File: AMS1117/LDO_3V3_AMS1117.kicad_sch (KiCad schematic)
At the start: 5 parts, among them U1 AMS1117-3.3

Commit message: added gnd
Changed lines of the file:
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@@
+	(wire
+		(pts
+			(xy 170.18 110.49) (xy 170.18 109.22)
+		)
+		(stroke
+			(width 0)
+			(type default)
+		)
+	)
 	(wire
 		(pts
@@
 		(pts
 			(xy 163.83 95.25) (xy 163.83 96.52)
+		)
+		(stroke
+			(width 0)
+			(type default)
+		)
+	)
+	(wire
+		(pts
+			(xy 170.18 109.22) (xy 172.72 109.22)
 		)
 		(stroke
@@
 		(shape input)
 		(at 125.73 95.25 90)
+		(fields_autoplaced yes)
+		(effects
+			(font
+				(size 1.27 1.27)
+			)
+			(justify left)
+		)
+	)
+	(hierarchical_label "GND"
+		(shape bidirectional)
+		(at 172.72 109.22 0)
 		(fields_autoplaced yes)
 		(effects
@@
 					(unit 1)
 				)
+			)
+		)
+	)
+	(symbol
+		(lib_id "power:GND")
+		(at 170.18 110.49 0)
+		(unit 1)
+		(exclude_from_sim no)
+		(in_bom yes)
+		(on_board yes)
+		(dnp no)
+		(property "Reference" "#PWR01"
+			(at 170.18 116.84 0)
+			(effects
+				(font
+					(size 1.27 1.27)
+				)
+				(hide yes)
+			)
+		)
+		(property "Value" "GND"
+			(at 170.307 114.8842 0)
+			(effects
+				(font
+					(size 1.27 1.27)
+				)
+			)
+		)
+		(property "Footprint" ""
+			(at 170.18 110.49 0)
+			(effects
+				(font
+					(size 1.27 1.27)
+				)
+				(hide yes)
+			)
+		)
+		(property "Datasheet" ""
+			(at 170.18 110.49 0)
+			(effects
+				(font
+					(size 1.27 1.27)
+				)
+				(hide yes)
+			)
+		)
+		(property "Description" ""
+			(at 170.18 110.49 0)
+			(effects
+				(font
+					(size 1.27 1.27)
+				)
+				(hide yes)
+			)
+		)
+		(pin "1"
+		)
+		(instances
+			(project "AMS1117"
+				(path "/d6eee423-2a55-45ad-a749-7df2395c1501/18c18bcb-7cad-4433-83e1-269ce5efd3b2"
+					(reference "#PWR01")
+					(unit 1)
+				)

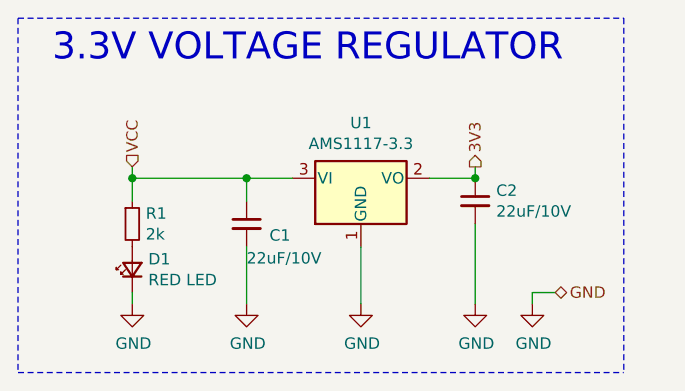
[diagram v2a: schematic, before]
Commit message: changes in, out for ams1117
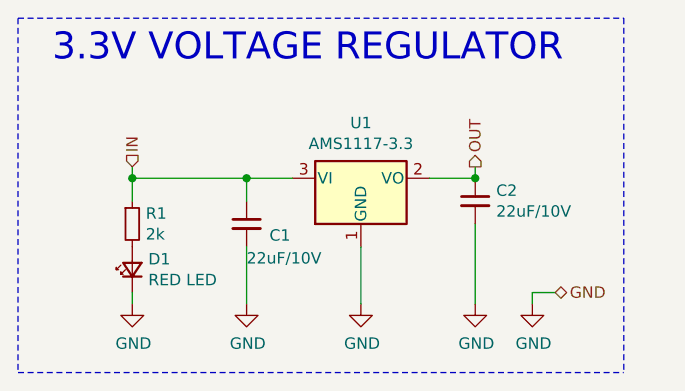
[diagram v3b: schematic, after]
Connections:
- net 3V3 renamed OUT
- net VCC renamed IN
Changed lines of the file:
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@@
 		)
 	)
-	(hierarchical_label "VCC"
+	(hierarchical_label "IN"
 		(shape input)
 		(at 125.73 95.25 90)
@@
 		)
 	)
-	(hierarchical_label "3V3"
+	(hierarchical_label "OUT"
 		(shape output)
 		(at 163.83 95.25 90)

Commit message: added json source
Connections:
- net IN renamed PIN
- net OUT renamed POUT
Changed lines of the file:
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@@
 		)
 	)
-	(hierarchical_label "IN"
+	(hierarchical_label "PIN"
 		(shape input)
 		(at 125.73 95.25 90)
@@
 		)
 	)
-	(hierarchical_label "OUT"
+	(hierarchical_label "POUT"
 		(shape output)
 		(at 163.83 95.25 90)
@@
 			(at 125.73 101.6 0)
 			(effects
+				(font
+					(size 1.27 1.27)
+				)
+				(hide yes)
+			)
+		)
+		(property "LCSC#" ""
+			(at 125.73 101.6 0)
+			(effects
